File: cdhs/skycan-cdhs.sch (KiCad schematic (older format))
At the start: 48 parts, among them J1 DF9-25P-1V-PLUG, J2 DF9-25P-1V-SOCKET, J3 DF9-25P-1V-PLUG, J4 DF9-25P-1V-SOCKET, P1 CONN_3X2, SW1 SW_PUSH_4_PIN, U1 MSP430F5528IRGCT, U2 MICRO-B_USB, U3 FM24CL04B, U4 SST25VF080B, X1 32.768kHz, X2 4MHz

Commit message: Now CDHS uses only skycan lib Mounting holes connected to gnd
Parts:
- removed J1, J3: DF9-25P-1V-PLUG, symbol DF9-25P-1V-PLUG
- removed J2, J4: DF9-25P-1V-SOCKET, symbol DF9-25P-1V-SOCKET
- removed U1: MSP430F5528IRGCT, andrew/b3kma, symbol 1144-MSP430F5528IRGCT
- added J1, J3: DF9_25P_1V_PLUG, symbol DF9_25P_1V_PLUG
- added J2, J4: DF9_25P_1V_SOCKET, symbol DF9_25P_1V_SOCKET
- added U1: MSP430F5528IRGCT, symbol MSP430F5528IRGCT
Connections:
- wire segments 144 -> 202

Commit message: Added Farnell codes and footprints to CDHS schematic
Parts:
- removed SW1: SW_PUSH_4_PIN, symbol SW_PUSH_4_PIN
- added SW1: SWITCH_4PIN, symbol SWITCH_4PIN
- C1, C11, C12, C13, C14, C15, C16, C17, C18, C19, C5, C7, C8, C9, R1, R10, R11, R2, R3, R4, R5, R6, R7, R8, R9: footprint (none) -> 0402
- C10, C4, C6, D2, D3, D4: footprint (none) -> 0603
- D1: Farnell (none) -> 1056832
- J1, J3: footprint (none) -> 1 mm 2 rows 25 pins; Farnell (none) -> 1798379
- J2, J4: footprint (none) -> 1 mm 2 rows 25 pins; Farnell (none) -> 1798380
- P1: footprint (none) -> smd 2x3 1.27 mm
- U1: footprint (none) -> VQFN64; Farnell (none) -> 1866820
- U2: footprint (none) -> 5 pads; Farnell (none) -> 2293753
- U3: footprint (none) -> SOIC8; Farnell (none) -> 2077746
- U4: footprint (none) -> SOIC8; Farnell (none) -> 1871942
- X1: footprint ABS10 -> 4.9 x 1.8 mm; Farnell (none) -> 2101352
- X2: footprint (none) -> HC49; Farnell (none) -> 1652553
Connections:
- wire segments 202 -> 144

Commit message: Added diode footprint info to CDHS
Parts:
- D1: footprint (none) -> SOT-23
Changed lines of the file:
@@
 F 0 "D1" H 4050 9550 40  0000 C CNN
 F 1 "DIODESCH3PIN" H 3750 9500 40  0001 C CNN
-F 2 "" H 4050 9450 60  0000 C CNN
+F 2 "SOT-23" H 4050 9450 60  0001 C CNN
 F 3 "http://ee.farnell.com/avago-technologies/hsms-2800-tr1g/diode-rf-schottky-sot-23/dp/1056832" H 4050 9450 60  0001 C CNN
 F 4 "1056832" H 4050 9450 60  0001 C CNN "Farnell"

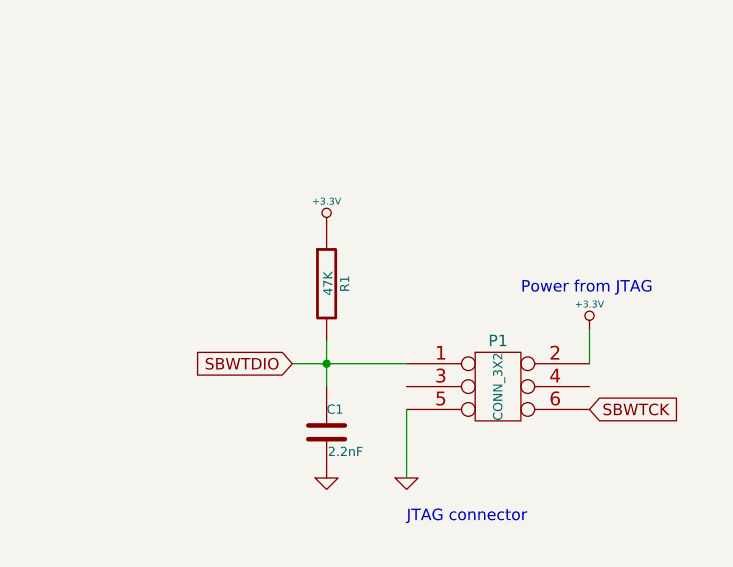
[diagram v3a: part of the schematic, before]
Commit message: Updated CDHS BOM
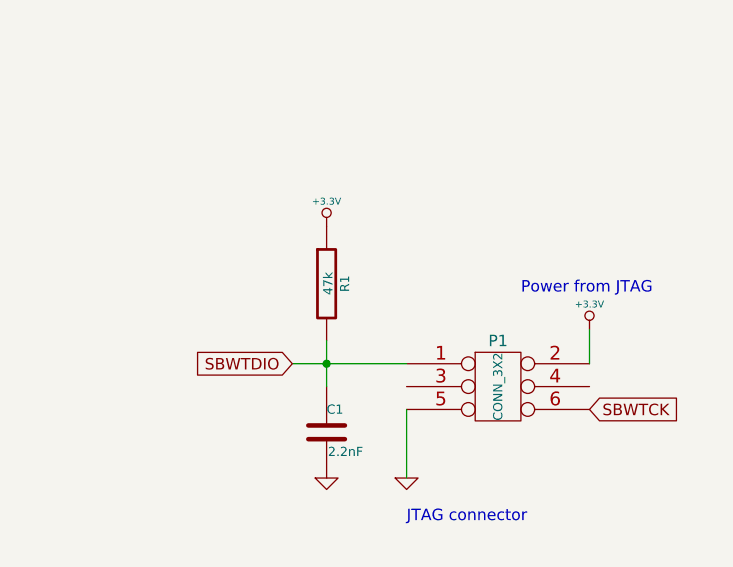
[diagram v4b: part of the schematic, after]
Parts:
- R1: value 47K -> 47k
- R6: Farnell (none) -> 2072645
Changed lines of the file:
@@
 P 3100 7050
 F 0 "R1" V 3180 7050 40  0000 C CNN
-F 1 "47K" V 3107 7051 40  0000 C CNN
+F 1 "47k" V 3107 7051 40  0000 C CNN
 F 2 "0402" V 3030 7050 30  0001 C CNN
 F 3 "" H 3100 7050 30  0000 C CNN
@@
 F 2 "0402" V 4280 9100 30  0001 C CNN
 F 3 "" H 4350 9100 30  0000 C CNN
+F 4 "2072645" V 4350 9100 60  0001 C CNN "Farnell"
 	1    4350 9100
 	1    0    0    -1

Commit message: Changed CDHS reset switch Farnell code
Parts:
- SW1: Farnell 2056841 -> 2056843
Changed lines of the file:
@@
 F 1 "SWITCH_4PIN" H 4050 8550 50  0000 C CNN
 F 2 "" H 4050 8750 60  0000 C CNN
-F 3 "http://ee.farnell.com/alps/skqgace010/switch-2-55n-5-2x5-2mm-no-actuator/dp/2056841" H 4050 8750 60  0001 C CNN
-F 4 "2056841" H 4050 8750 60  0001 C CNN "Farnell"
+F 3 "http://www.farnell.com/datasheets/1582326.pdf" H 4050 8750 60  0001 C CNN
+F 4 "2056843" H 4050 8750 60  0001 C CNN "Farnell"
 	1    4050 8750
 	1    0    0    -1
